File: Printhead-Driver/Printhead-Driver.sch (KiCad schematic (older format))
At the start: 50 parts, among them J1 IDC_Connector, J2 2 x 10 Pinheader, U1 TMI8870B, U2 TMI8870B, U3 TMI8870B, U4 TMI8870B, U5 TMI8870B, U6 TMI8870B, U7 TMI8870B, U8 TMI8870B

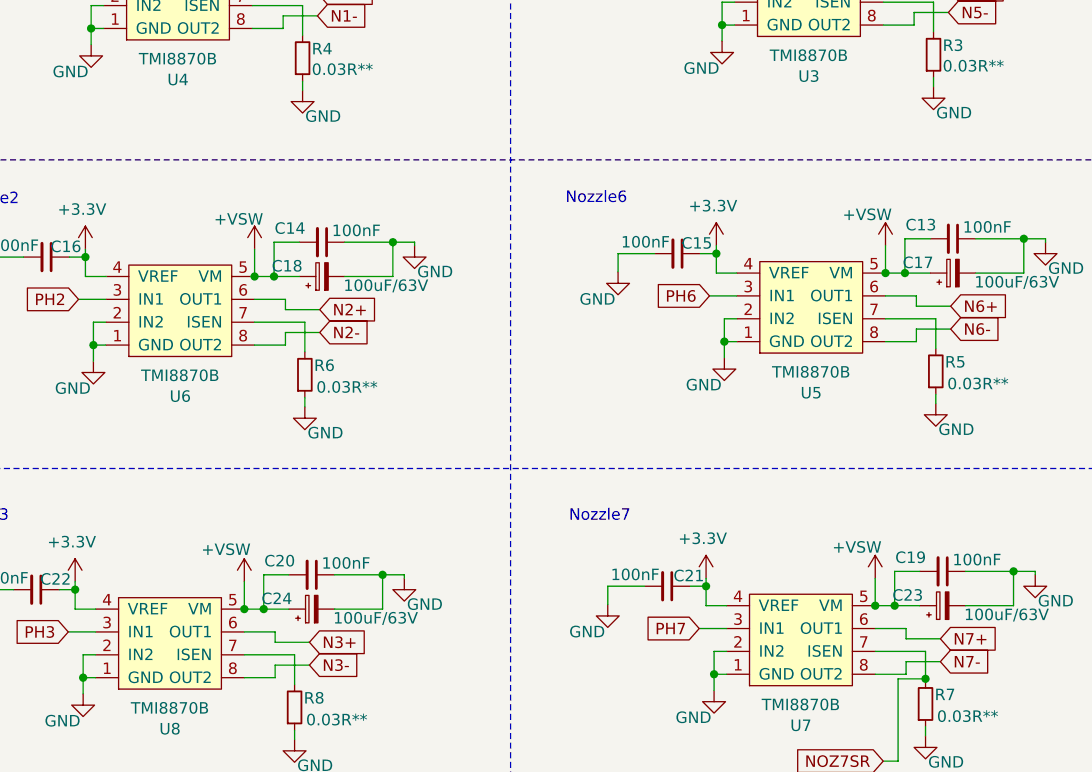
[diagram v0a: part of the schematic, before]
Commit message: final PCB KiCAD design files for V0.5 as sent off for manufacture at JLCPCB 2022-03-22
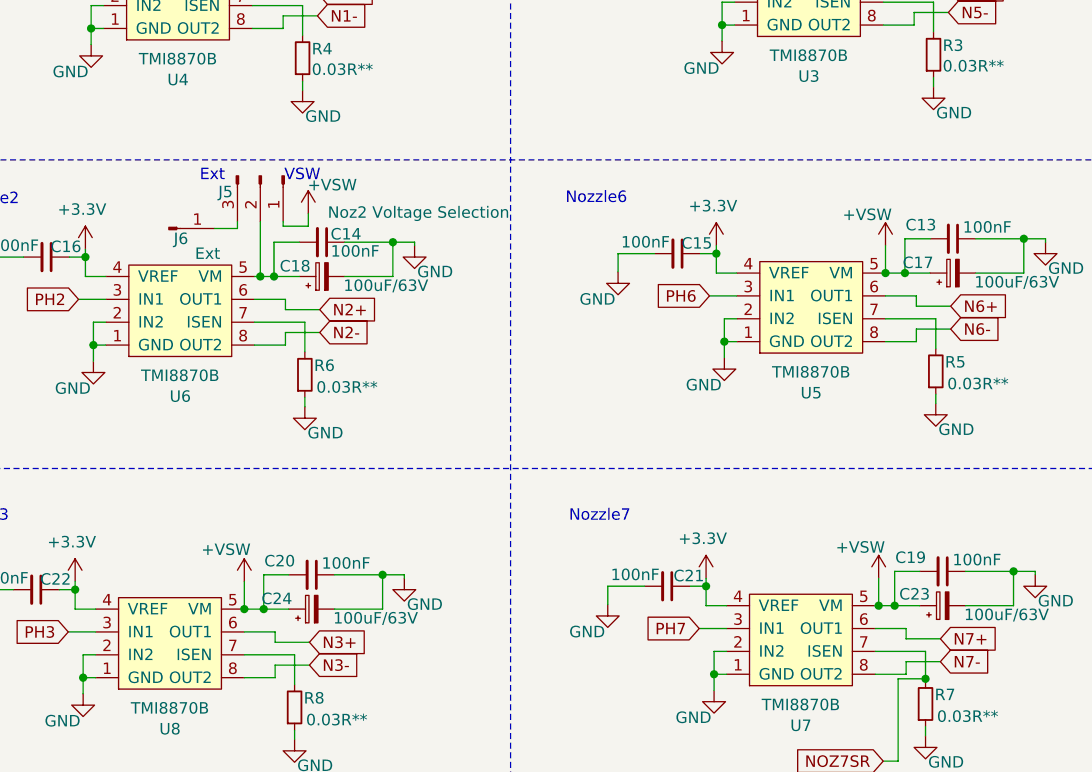
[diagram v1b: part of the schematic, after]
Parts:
- added J5: Noz2 Voltage Selection, Connector_PinHeader_2.54mm:PinHeader_1x03_P2.54mm_Vertical, symbol Connector:Conn_01x03_Male
- added J6: Ext, Connector_PinHeader_2.54mm:PinHeader_1x01_P2.54mm_Vertical, symbol Connector:Conn_01x01_Male
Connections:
- net +VSW: now also J5.1 (Pin_1); no longer C14.2, C18.1, U6.5 (VM)
- new net: C14.2, C18.1, J5.2 (Pin_2), U6.5 (VM)
- new net: J5.3 (Pin_3), J6.1 (Pin_1)
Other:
- note added: "Ext"
- note added: "VSW"
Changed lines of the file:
@@
 encoding utf-8
 Sheet 1 2
-Title ""
-Date "2022-03-18"
-Rev "0.5c1"
+Title "Open-PyroJet-Driver"
+Date "2022-03-22"
+Rev "0.5c2"
 Comp "PRL"
 Comment1 "Open Hardware"
@@
 Wire Wire Line
 	2810 4235 3030 4235
-Wire Wire Line
-	2810 4035 2810 3915
-$Comp
-L power:+VSW #PWR?
-U 1 1 6313E9CC
-P 2810 3915
-AR Path="/6229DCDC/6313E9CC" Ref="#PWR?"  Part="1"
-AR Path="/62560F5D/6313E9CC" Ref="#PWR?"  Part="1"
-AR Path="/629B5586/6313E9CC" Ref="#PWR?"  Part="1"
-AR Path="/630E7389/6313E9CC" Ref="#PWR?"  Part="1"
-AR Path="/6313E9CC" Ref="#PWR031"  Part="1"
-F 0 "#PWR031" H 2810 3765 50  0001 C CNN
-F 1 "+VSW" H 2880 4045 50  0000 C CNN
-F 2 "" H 2810 3915 50  0001 C CNN
-F 3 "" H 2810 3915 50  0001 C CNN
-	1    2810 3915
-	-1   0    0    -1
-$EndComp
 $Comp
 L Device:R_Small R6
@@
 AR Path="/630E7389/6313EA37" Ref="C?"  Part="1"
 AR Path="/6313EA37" Ref="C14"  Part="1"
-F 0 "C14" V 3045 3745 50  0000 C CNN
-F 1 "100nF" V 3055 4035 50  0000 C CNN
+F 0 "C14" V 3070 3990 50  0000 C CNN
+F 1 "100nF" V 3145 4030 50  0000 C CNN
 F 2 "Capacitor_SMD:C_0603_1608Metric" H 3105 3885 50  0001 C CNN
 F 3 "~" H 3105 3885 50  0001 C CNN
@@
 $EndComp
 Wire Wire Line
-	2810 4035 2895 4035
+	2810 4035 2835 4035
 Wire Wire Line
 	3005 3885 2895 3885
@@
 	-1   0    0    -1
 $EndComp
-Connection ~ 2810 4035
 Connection ~ 2800 2650
 $Comp
@@
 Wire Wire Line
 	5525 5675 5745 5675
-Wire Wire Line
-	5525 5475 5525 5355
 $Comp
 L power:+VSW #PWR?
 U 1 1 6313EC31
-P 5525 5355
+P 3045 3760
 AR Path="/6229DCDC/6313EC31" Ref="#PWR?"  Part="1"
 AR Path="/62560F5D/6313EC31" Ref="#PWR?"  Part="1"
@@
 AR Path="/630E7389/6313EC31" Ref="#PWR?"  Part="1"
 AR Path="/6313EC31" Ref="#PWR042"  Part="1"
-F 0 "#PWR042" H 5525 5205 50  0001 C CNN
-F 1 "+VSW" H 5605 5490 50  0000 C CNN
-F 2 "" H 5525 5355 50  0001 C CNN
-F 3 "" H 5525 5355 50  0001 C CNN
-	1    5525 5355
+F 0 "#PWR042" H 3045 3610 50  0001 C CNN
+F 1 "+VSW" H 2940 3885 50  0000 C CNN
+F 2 "" H 3045 3760 50  0001 C CNN
+F 3 "" H 3045 3760 50  0001 C CNN
+	1    3045 3760
 	-1   0    0    -1
 $EndComp
@@
 $EndComp
 Wire Wire Line
-	5525 5475 5610 5475
+	5525 5475 5540 5475
 Wire Wire Line
 	5720 5325 5610 5325
@@
 	-1   0    0    -1
 $EndComp
-Connection ~ 5525 5475
 $Comp
 L Device:C_Small C?
@@
 AR Path="/630E7112/62635BDD" Ref="C?"  Part="1"
 AR Path="/62635BDD" Ref="C23"  Part="1"
-F 0 "C23" V 5865 5560 50  0000 L CNN
+F 0 "C23" V 5870 5530 50  0000 L CNN
 F 1 "100uF/63V" V 5780 5010 50  0000 L CNN
 F 2 "Capacitor_THT:CP_Radial_D8.0mm_P3.50mm" H 5820 5475 50  0001 C CNN
@@
 AR Path="/630E7112/626370C1" Ref="C?"  Part="1"
 AR Path="/626370C1" Ref="C18"  Part="1"
-F 0 "C18" V 3150 4120 50  0000 L CNN
+F 0 "C18" V 3150 4085 50  0000 L CNN
 F 1 "100uF/63V" V 3065 3570 50  0000 L CNN
 F 2 "Capacitor_THT:CP_Radial_D8.0mm_P3.50mm" H 3105 4035 50  0001 C CNN
@@
 	1    0    0    -1
 $EndComp
+Text Notes 2940 3625 0    50   ~ 0
+VSW
+Text Notes 2570 3625 0    50   ~ 0
+Ext
+Wire Wire Line
+	2935 3795 2935 3815
+Wire Wire Line
+	2935 3815 3045 3815
+Wire Wire Line
+	3045 3815 3045 3760
+$Comp
+L Connector:Conn_01x03_Male J?
+U 1 1 625AC358
+P 2835 3595
+AR Path="/630E7112/625AC358" Ref="J?"  Part="1"
+AR Path="/625AC358" Ref="J5"  Part="1"
+F 0 "J5" V 2905 3475 50  0000 R CNN
+F 1 "Noz2 Voltage Selection" V 2995 4685 50  0000 R CNN
+F 2 "Connector_PinHeader_2.54mm:PinHeader_1x03_P2.54mm_Vertical" H 2835 3595 50  0001 C CNN
+F 3 "~" H 2835 3595 50  0001 C CNN
+	1    2835 3595
+	0    1    1    0
+$EndComp
+$Comp
+L Connector:Conn_01x01_Male J?
+U 1 1 626245B7
+P 2435 3825
+AR Path="/630E7112/626245B7" Ref="J?"  Part="1"
+AR Path="/626245B7" Ref="J6"  Part="1"
+F 0 "J6" H 2520 3780 50  0000 R CNN
+F 1 "Ext" H 2660 3715 50  0000 R CNN
+F 2 "Connector_PinHeader_2.54mm:PinHeader_1x01_P2.54mm_Vertical" H 2435 3825 50  0001 C CNN
+F 3 "~" H 2435 3825 50  0001 C CNN
+	1    2435 3825
+	1    0    0    -1
+$EndComp
+Wire Wire Line
+	2735 3795 2735 3825
+Wire Wire Line
+	2735 3825 2635 3825
+Wire Wire Line
+	2835 3795 2835 4035
+Connection ~ 2835 4035
+Wire Wire Line
+	2835 4035 2895 4035
+Wire Wire Line
+	5540 5475 5540 5355
+$Comp
+L power:+VSW #PWR?
+U 1 1 6271D937
+P 5540 5355
+AR Path="/6229DCDC/6271D937" Ref="#PWR?"  Part="1"
+AR Path="/62560F5D/6271D937" Ref="#PWR?"  Part="1"
+AR Path="/629B5586/6271D937" Ref="#PWR?"  Part="1"
+AR Path="/630E7389/6271D937" Ref="#PWR?"  Part="1"
+AR Path="/6271D937" Ref="#PWR0105"  Part="1"
+F 0 "#PWR0105" H 5540 5205 50  0001 C CNN
+F 1 "+VSW" H 5620 5490 50  0000 C CNN
+F 2 "" H 5540 5355 50  0001 C CNN
+F 3 "" H 5540 5355 50  0001 C CNN
+	1    5540 5355
+	-1   0    0    -1
+$EndComp
+Connection ~ 5540 5475
+Wire Wire Line
+	5540 5475 5610 5475
 $EndSCHEMATC

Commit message: Updating Controller and Driver boards to version 0.6
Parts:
- removed C1, C19, C2, C20: 100nF, Capacitor_SMD:C_0603_1608Metric, symbol Device:C_Small
- removed J2: 2 x 10 Pinheader, Connector_PinHeader_2.54mm:PinHeader_2x10_P2.54mm_Vertical, symbol Connector_Generic:Conn_02x10_Odd_Even
- removed J5: Noz2 Voltage Selection, Connector_PinHeader_2.54mm:PinHeader_1x03_P2.54mm_Vertical, symbol Connector:Conn_01x03_Male
- removed J6: Ext, Connector_PinHeader_2.54mm:PinHeader_1x01_P2.54mm_Vertical, symbol Connector:Conn_01x01_Male
- added C15, C16, C23, C24, C31, C32: 100nF, Capacitor_SMD:C_0603_1608Metric, symbol Device:C_Small
- added C21, C22, C29, C30, C5: 1nF**, Capacitor_SMD:C_0603_1608Metric, symbol Device:C_Small
- added C6: 1nF**DNF, Capacitor_SMD:C_0603_1608Metric, symbol Device:C_Small
- added J2: Controller, Connector_PinHeader_2.54mm:PinHeader_2x12_P2.54mm_Vertical, symbol Connector_Generic:Conn_02x12_Odd_Even
- added U11, U12, U15, U16, U3, U7, U8: INA180, Package_TO_SOT_SMD:SOT-23-5, symbol Pauls_Symbol_Library:INA180
- added U4: INA180-DNF, Package_TO_SOT_SMD:SOT-23-5, symbol Pauls_Symbol_Library:INA180
- C13, C14: value 100nF -> 1nF**
- C8: value 100nF -> 100nF-DNF
- R1, R2, R3, R4, R5, R6, R7, R8: footprint Resistor_SMD:R_2512_6332Metric -> Resistor_SMD:R_1206_3216Metric
- renumbered C5 to C1, C12 to C10, C9 to C11, C10 to C12, C15 to C19, C6 to C2, C16 to C20, C23 to C25, C24 to C26, C21 to C27, C22 to C28, C11 to C9, TP7 to TP3, TP8 to TP4, U6 to U10, U7 to U13, U8 to U14, U3 to U5, U4 to U6, U5 to U9
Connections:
- net +3V3: now also J2.13 (Pin_13), J2.9 (Pin_9)
- net +VSW: now also C18.1, U10.5 (VM); no longer C13.2, C7.2, C8.2
- net GND: now also C7.2, C8.2, C15.2, C16.2, C21.1, C22.1, C23.2, C24.2, C29.1, C30.1, C31.2, C32.2, C5.1, C6.1, J2.1 (Pin_1), J2.11 (Pin_11), J2.15 (Pin_15), J2.17 (Pin_17), J2.19 (Pin_19), J2.21 (Pin_21), J2.23 (Pin_23), J2.3 (Pin_3), J2.5 (Pin_5), J2.7 (Pin_7), U11.2 (GND), U11.4 (IN-), U12.2 (GND), U12.4 (IN-), U15.2 (GND), U15.4 (IN-), U16.2 (GND), U16.4 (IN-), U3.2 (GND), U3.4 (IN-), U4.2 (GND), U4.4 (IN-), U7.2 (GND), U7.4 (IN-), U8.2 (GND), U8.4 (IN-); no longer C7.1, C8.1
- net PH0: now also J2.2 (Pin_2)
- net PH1: now also J2.4 (Pin_4)
- net PH2: now also J2.6 (Pin_6)
- net PH3: now also J2.8 (Pin_8)
- net PH4: now also J2.10 (Pin_10)
- net PH5: now also J2.12 (Pin_12)
- net PH6: now also J2.14 (Pin_14)
- net PH7: now also J2.16 (Pin_16)
- net at R2.2, U2.7 (ISEN): now also C6.2, U4.3 (IN+)
- net at R4.2, U6.7 (ISEN): now also C14.2, U8.3 (IN+)
- net at R6.2, U10.7 (ISEN): now also C22.2, U12.3 (IN+)
- net at R8.2, U14.7 (ISEN): now also C30.2, U16.3 (IN+)
- net at R1.2, U1.7 (ISEN): now also C5.2, U3.3 (IN+)
- net at R3.2, U5.7 (ISEN): now also C13.2, U7.3 (IN+)
- net at R5.2, U9.7 (ISEN): now also C21.2, U11.3 (IN+)
- net NOZ7SR: no longer names the net of R7.2, U13.7 (ISEN)
- net NOZ7SR: now also C29.2, U15.3 (IN+)
- new net +5V: C15.1, C16.1, C23.1, C24.1, C31.1, C32.1, C7.1, C8.1, U11.5 (VS), U12.5 (VS), U15.5 (VS), U16.5 (VS), U3.5 (VS), U4.5 (VS), U7.5 (VS), U8.5 (VS)
- new net CS: J2.24 (Pin_24)
- new net MISO: J2.20 (Pin_20)
- new net MOSI: J2.22 (Pin_22)
- new net NR1: U8.1 (OUT)
- new net NR2: U12.1 (OUT)
- new net NR3: U16.1 (OUT)
- new net NR4: U3.1 (OUT)
- new net NR5: U7.1 (OUT)
- new net NR6: U11.1 (OUT)
- new net NR7: U15.1 (OUT)
- new net SLCK: J2.18 (Pin_18)
- no-connect marks 0 -> 1
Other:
- note added: "** this part value will need testing\nMight need to be: 0.02, 0.03, 0.04 or 0.05 Ohms\nDepends on final Filament Resistance"
- note added: "Note: Nozzle 0 isn't monitored as \nthe ADC pin is being used to \nmeasure the Motor Drive voltage. \nFootprints are being placed just in \ncase though"
- note removed: "** this part value will need testing"
- note removed: "Ext"
- note removed: "NOTE: ADD MORE TEST POINTS and a jumper on a nozzle sense resistor --> the ADC\n"
- note removed: "VSW"
- moved on the sheet: C1, C10, C11, C12, C17, C18, C19, C2, C20, C25, C26, C27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

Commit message: Adding in version 0.7 KiACD design files
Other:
- note added: "Motor Driver H-Bridge IC:\n------------------\nAT8870 - 38V 3.6A, 29K STK, A$1.25/30\nRZ7899 - 25V 6A 84K STK, A$0.51/30 (no sense resistor)\nHV8548 - 28V 1.2A-2.4A, 5K STK, A$0.78/30\nPT2470 - 36V 3.6A, 2.5K STK, A0.80/30\nTMI8870B - 45V 3.6A, 3.5K STK, A$0.90/30 (up to 100KHz PWM = 10uSec pules)"
- note removed: "Motor Driver H-Bridge IC:\n------------------\nAT8870 - 38V 3.6A, 29K STK, A$1.25/30\nRZ7899 - 25V 6A 84K STK, A$0.51/30\nHV8548 - 28V 1.2A-2.4A, 5K STK, A$0.78/30\nPT2470 - 36V 3.6A, 2.5K STK, A0.80/30\nTMI8870B - 45V 3.6A, 3.5K STK, A$0.90/30 (up to 100KHz PWM = 10uSec pules)"
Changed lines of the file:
@@
 Sheet 1 2
 Title "Open-PyroJet-Driver"
-Date "2022-05-11"
-Rev "0.6a"
+Date "2022-06-12"
+Rev "0.7"
 Comp "PRL"
 Comment1 "Open Hardware"
@@
 	2380 4610 2380 4575
 Text Notes 7535 6335 0    50   ~ 0
-Motor Driver H-Bridge IC:\n------------------\nAT8870 - 38V 3.6A, 29K STK, A$1.25/30\nRZ7899 - 25V 6A 84K STK, A$0.51/30\nHV8548 - 28V 1.2A-2.4A, 5K STK, A$0.78/30\nPT2470 - 36V 3.6A, 2.5K STK, A0.80/30\nTMI8870B - 45V 3.6A, 3.5K STK, A$0.90/30 (up to 100KHz PWM = 10uSec pules)
+Motor Driver H-Bridge IC:\n------------------\nAT8870 - 38V 3.6A, 29K STK, A$1.25/30\nRZ7899 - 25V 6A 84K STK, A$0.51/30 (no sense resistor)\nHV8548 - 28V 1.2A-2.4A, 5K STK, A$0.78/30\nPT2470 - 36V 3.6A, 2.5K STK, A0.80/30\nTMI8870B - 45V 3.6A, 3.5K STK, A$0.90/30 (up to 100KHz PWM = 10uSec pules)
 $Comp
 L Pauls_Symbol_Library:TMI8870B U?
